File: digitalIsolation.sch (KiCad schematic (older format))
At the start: 9 parts, among them U14 74AHC1G14, U15 Si8651

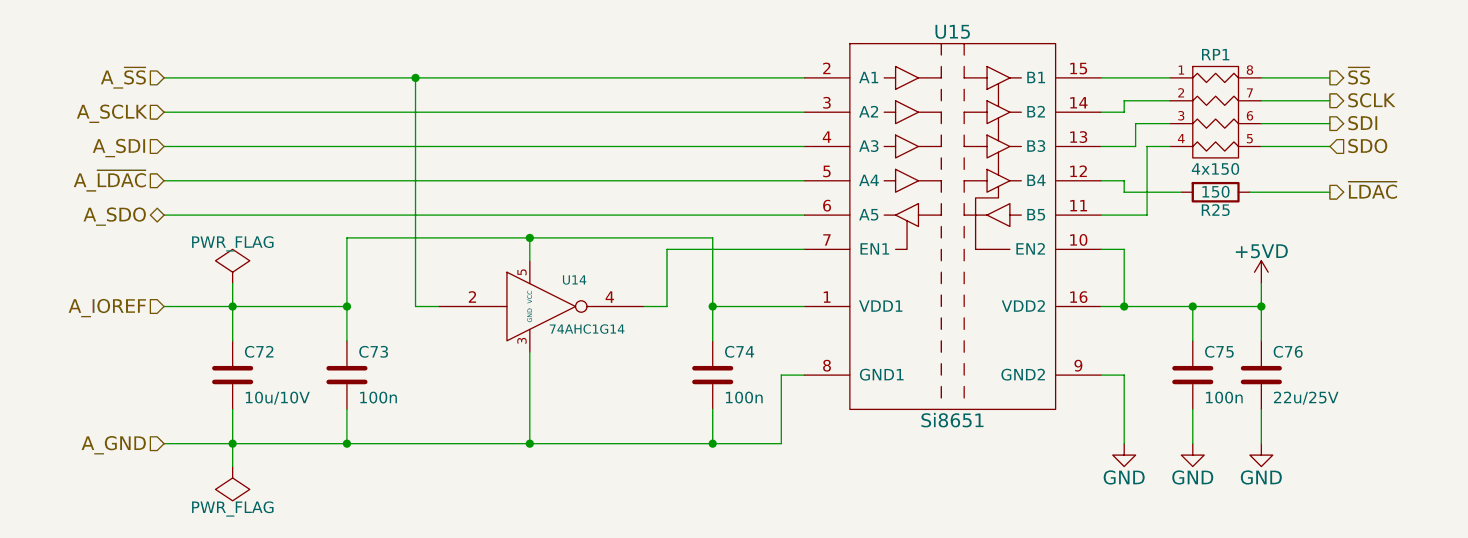
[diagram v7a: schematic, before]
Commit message: Re-referenced components
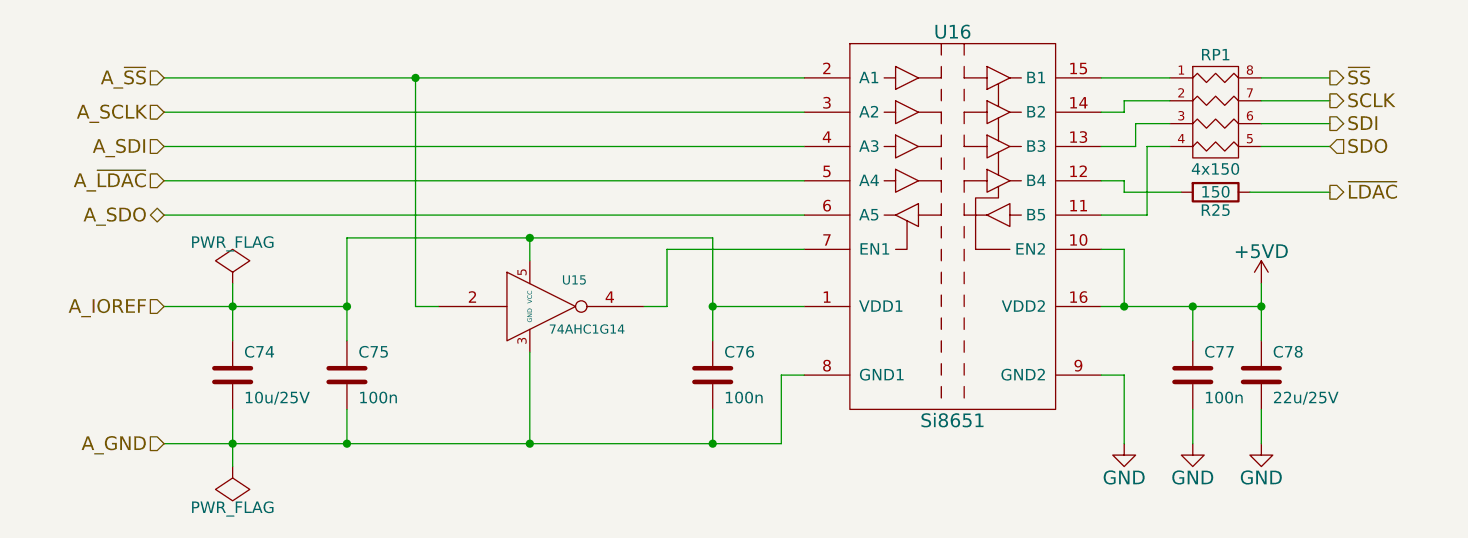
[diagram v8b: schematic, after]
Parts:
- removed C72: 10u/10V, Capacitors_SMD:C_0805, symbol C
- added C74: 10u/25V, Capacitors_SMD:C_0805, symbol C
- renumbered C73 to C75, C74 to C76, C75 to C77, C76 to C78, U14 to U15, U15 to U16
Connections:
- net A_GND: now also C74.2
- net A_IOREF: now also C74.1
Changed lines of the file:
@@
 ~LDAC
 $Comp
-L Si8651 U15
+L Si8651 U16
 U 1 1 5574AB03
 P 7050 2850
-F 0 "U15" H 7050 3700 60  0000 C CNN
+F 0 "U16" H 7050 3700 60  0000 C CNN
 F 1 "Si8651" H 7050 2000 60  0000 C CNN
 F 2 "Housings_SOIC:SOIC-16_3.9x9.9mm_Pitch1.27mm" H 7050 3050 60  0001 C CNN
@@
 	8100 3650 8100 3800
 $Comp
-L GND #PWR85
+L GND #PWR089
 U 1 1 5574AC81
 P 7800 3800
-F 0 "#PWR85" H 7800 3550 60  0001 C CNN
+F 0 "#PWR089" H 7800 3550 60  0001 C CNN
 F 1 "GND" H 7800 3650 60  0000 C CNN
 F 2 "" H 7800 3800 60  0000 C CNN
@@
 $EndComp
 $Comp
-L GND #PWR86
+L GND #PWR090
 U 1 1 5574ACAE
 P 8100 3800
-F 0 "#PWR86" H 8100 3550 60  0001 C CNN
+F 0 "#PWR090" H 8100 3550 60  0001 C CNN
 F 1 "GND" H 8100 3650 60  0000 C CNN
 F 2 "" H 8100 3800 60  0000 C CNN
@@
 $EndComp
 $Comp
-L 74AHC1G14 U14
+L 74AHC1G14 U15
 U 1 1 5574ACE6
 P 5250 3200
-F 0 "U14" H 5395 3315 40  0000 C CNN
+F 0 "U15" H 5395 3315 40  0000 C CNN
 F 1 "74AHC1G14" H 5450 3100 40  0000 C CNN
 F 2 "Housings_SOT-23_SOT-143_TSOT-6:SOT-23-5" H 5345 3065 30  0001 C CNN
@@
 Text HLabel 3600 3800 0    60   Input ~ 0
 A_GND
-$Comp
-L C C72
-U 1 1 5574B7E4
-P 3900 3500
-F 0 "C72" H 3950 3600 50  0000 L CNN
-F 1 "10u/10V" H 3950 3400 50  0000 L CNN
-F 2 "Capacitors_SMD:C_0805" H 3938 3350 30  0001 C CNN
-F 3 "" H 3900 3500 60  0000 C CNN
-F 4 "GRM21BR61A106KE19L" H 3900 3500 60  0001 C CNN "Part Number"
-F 5 "Murata" H 3900 3500 60  0001 C CNN "Manufacturer"
-F 6 "0805" H 3900 3500 60  0001 C CNN "Package"
-F 7 "Farnell" H 3900 3500 60  0001 C CNN "Supplier"
-F 8 "1828805" H 3900 3500 60  0001 C CNN "Order Code"
-F 9 "Mouser" H 3900 3500 60  0001 C CNN "Alt. Supplier"
-F 10 "603-CC805KKX5R8BB106" H 3900 3500 60  0001 C CNN "Alt. Order Code"
-F 11 "10μ/10V X5R 0805 ceramic capacitor" H 3900 3500 60  0001 C CNN "Note"
-	1    3900 3500
-	1    0    0    -1
-$EndComp
 Wire Wire Line
 	3900 3100 3900 3350
@@
 	7700 2200 8000 2200
 $Comp
-L C C76
+L C C78
 U 1 1 56E16574
 P 8400 3500
-F 0 "C76" H 8450 3600 50  0000 L CNN
+F 0 "C78" H 8450 3600 50  0000 L CNN
 F 1 "22u/25V" H 8450 3400 50  0000 L CNN
 F 2 "Capacitors_SMD:C_1210" H 8438 3350 30  0001 C CNN
@@
 Connection ~ 8400 3200
 $Comp
-L +5VD #PWR87
+L +5VD #PWR091
 U 1 1 5574AC36
 P 8400 3100
-F 0 "#PWR87" H 8400 2950 60  0001 C CNN
+F 0 "#PWR091" H 8400 2950 60  0001 C CNN
 F 1 "+5VD" H 8400 3240 60  0000 C CNN
 F 2 "" H 8400 3100 60  0000 C CNN
@@
 	8400 3650 8400 3800
 $Comp
-L GND #PWR88
+L GND #PWR092
 U 1 1 56E16784
 P 8400 3800
-F 0 "#PWR88" H 8400 3550 60  0001 C CNN
+F 0 "#PWR092" H 8400 3550 60  0001 C CNN
 F 1 "GND" H 8400 3650 60  0000 C CNN
 F 2 "" H 8400 3800 60  0000 C CNN
@@
 	7800 2700 8050 2700
 $Comp
-L PWR_FLAG #FLG8
+L PWR_FLAG #FLG093
 U 1 1 56F3D1DA
 P 3900 3100
-F 0 "#FLG8" H 3900 3195 50  0001 C CNN
+F 0 "#FLG093" H 3900 3195 50  0001 C CNN
 F 1 "PWR_FLAG" H 3900 3280 50  0000 C CNN
 F 2 "" H 3900 3100 50  0000 C CNN
@@
 $EndComp
 $Comp
-L PWR_FLAG #FLG9
+L PWR_FLAG #FLG094
 U 1 1 56F3D24A
 P 3900 3900
-F 0 "#FLG9" H 3900 3995 50  0001 C CNN
+F 0 "#FLG094" H 3900 3995 50  0001 C CNN
 F 1 "PWR_FLAG" H 3900 4080 50  0000 C CNN
 F 2 "" H 3900 3900 50  0000 C CNN
@@
 $EndComp
 $Comp
-L C C73
+L C C75
 U 1 1 56F34E94
 P 4400 3500
-F 0 "C73" H 4450 3600 50  0000 L CNN
+F 0 "C75" H 4450 3600 50  0000 L CNN
 F 1 "100n" H 4450 3400 50  0000 L CNN
 F 2 "Capacitors_SMD:C_0603" H 4438 3350 30  0001 C CNN
@@
 $EndComp
 $Comp
-L C C74
+L C C76
 U 1 1 56F3500A
 P 6000 3500
-F 0 "C74" H 6050 3600 50  0000 L CNN
+F 0 "C76" H 6050 3600 50  0000 L CNN
 F 1 "100n" H 6050 3400 50  0000 L CNN
 F 2 "Capacitors_SMD:C_0603" H 6038 3350 30  0001 C CNN
@@
 $EndComp
 $Comp
-L C C75
+L C C77
 U 1 1 56F35072
 P 8100 3500
-F 0 "C75" H 8150 3600 50  0000 L CNN
+F 0 "C77" H 8150 3600 50  0000 L CNN
 F 1 "100n" H 8150 3400 50  0000 L CNN
 F 2 "Capacitors_SMD:C_0603" H 8138 3350 30  0001 C CNN
@@
 	1    0    0    -1
 $EndComp
+$Comp
+L C C74
+U 1 1 56F2FB03
+P 3900 3500
+F 0 "C74" H 3950 3600 50  0000 L CNN
+F 1 "10u/25V" H 3950 3400 50  0000 L CNN
+F 2 "Capacitors_SMD:C_0805" H 3938 3350 30  0001 C CNN
+F 3 "" H 3900 3500 60  0000 C CNN
+F 4 "GRM219R61E106KA12D" H 3900 3500 60  0001 C CNN "Part Number"
+F 5 "Murata" H 3900 3500 60  0001 C CNN "Manufacturer"
+F 6 "0805" H 3900 3500 60  0001 C CNN "Package"
+F 7 "Farnell" H 3900 3500 60  0001 C CNN "Supplier"
+F 8 "2426961" H 3900 3500 60  0001 C CNN "Order Code"
+F 9 "Mouser" H 3900 3500 60  0001 C CNN "Alt. Supplier"
+F 10 "603-CC805KKX5R8BB106" H 3900 3500 60  0001 C CNN "Alt. Order Code"
+F 11 "10μF/25V X5R 0805 ceramic capacitor" H 3900 3500 60  0001 C CNN "Note"
+	1    3900 3500
+	1    0    0    -1
+$EndComp
